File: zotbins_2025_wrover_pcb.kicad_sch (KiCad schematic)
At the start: 6 parts, among them J1 ov2640, J2 hcsr04, J3 hx711, J4 infrared, U1 ESP32-WROVER-E/IE-DEVKIT-C, U2 MCP23017_SP

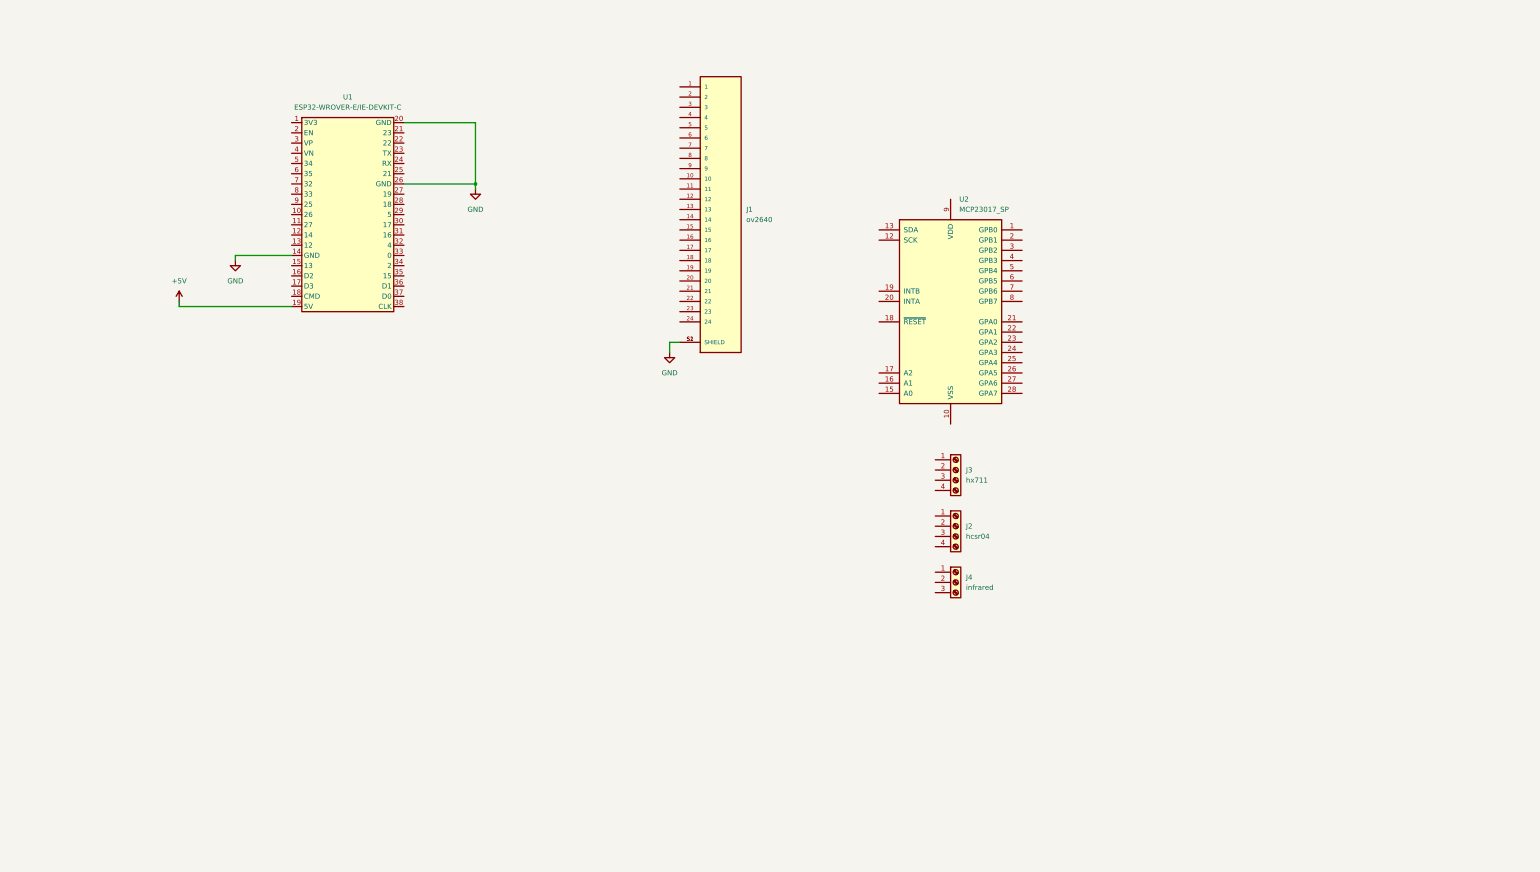
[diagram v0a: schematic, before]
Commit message: Camera and GPIO Expander sch updated
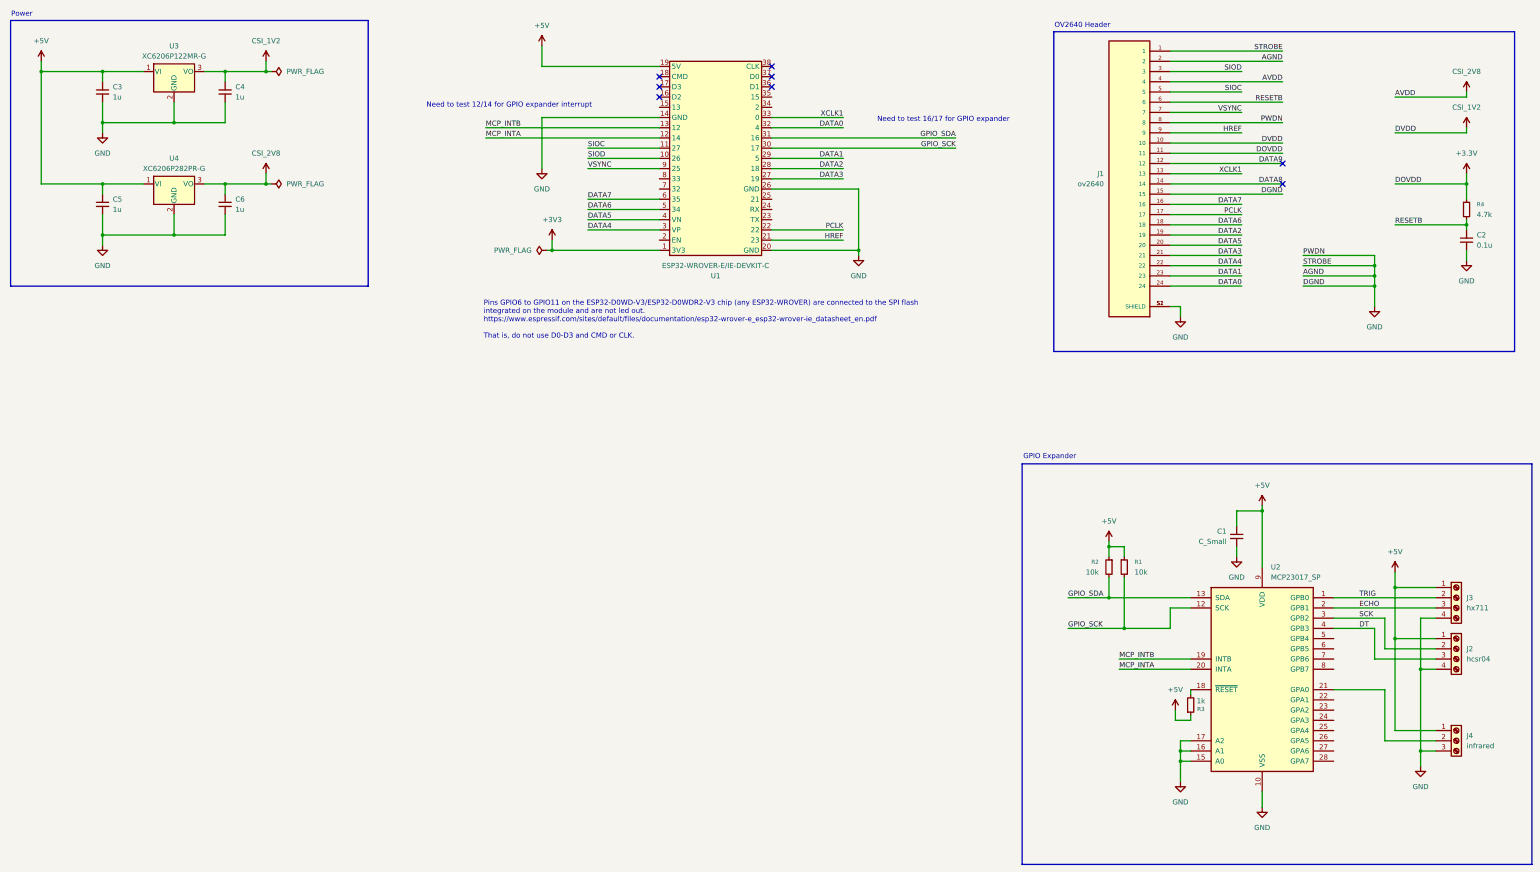
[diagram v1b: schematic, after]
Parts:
- added C1: C_Small, symbol Device:C_Small
- added C2: 0.1u, symbol Device:C_Small
- added C3, C4, C5, C6: 1u, symbol Device:C_Small
- added R1, R2: 10k, symbol Device:R_Small
- added R3: 1k, symbol Device:R_Small
- added R4: 4.7k, symbol Device:R_Small
- added U3: XC6206P122MR-G, Package_TO_SOT_THT:TO-220-3_Vertical, symbol Regulator_Linear:XC6206P122MR-G
- added U4: XC6206P282PR-G, Package_TO_SOT_THT:TO-220-3_Vertical, symbol Regulator_Linear:XC6206P282PR-G
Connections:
- net +5V: now also J2.1 (Pin_1), J3.1 (Pin_1), J4.1 (Pin_1), U2.9 (VDD), C1.1, C3.1, C5.1, R1.1, R2.1, R3.1, U3.1 (VI), U4.1 (VI)
- net GND: now also J1.1, J1.15, J1.2, J1.8, J2.4 (Pin_4), J3.4 (Pin_4), J4.3 (Pin_3), U2.10 (VSS), U2.15 (A0), U2.16 (A1), U2.17 (A2), C1.2, C2.2, C3.2, C4.2, C5.2, C6.2, U3.2 (GND), U4.2 (GND)
- net SCK: now reaches J2.2 (Pin_2)
- net SCK: now also U2.3 (GPB2)
- net DT: now reaches J2.3 (Pin_3)
- net DT: now also U2.4 (GPB3)
- net at J4.2 (Pin_2): now also U2.21 (GPA0)
- net +3V3: now reaches U1.1 (3V3)
- net SIOD: now reaches U1.10 (26)
- net SIOD: now also J1.3
- net SIOC: now reaches U1.11 (27)
- net SIOC: now also J1.5
- net MCP_INTA: now reaches U1.12 (14)
- net MCP_INTA: now also U2.20 (INTA)
- net MCP_INTB: now reaches U1.13 (12)
- net MCP_INTB: now also U2.19 (INTB)
- net HREF: now reaches U1.21 (23)
- net HREF: now also J1.9
- net PCLK: now reaches U1.22
- net PCLK: now also J1.17
- net DATA3: now reaches U1.27 (19)
- net DATA3: now also J1.21
- net DATA2: now reaches U1.28 (18)
- net DATA2: now also J1.19
- net DATA1: now reaches U1.29 (5)
- net DATA1: now also J1.23
- net DATA4: now reaches U1.3 (VP)
- net DATA4: now also J1.22
- net GPIO_SCK: now reaches U1.30 (17)
- net GPIO_SCK: now also U2.12 (SCK), R1.2
- net GPIO_SDA: now reaches U1.31 (16)
- net GPIO_SDA: now also U2.13 (SDA), R2.2
- net DATA0: now reaches U1.32 (4)
- net DATA0: now also J1.24
- net XCLK1: now reaches U1.33 (0)
- net XCLK1: now also J1.13
- net DATA5: now reaches U1.4 (VN)
- net DATA5: now also J1.20
- net DATA6: now reaches U1.5 (34)
- net DATA6: now also J1.18
- net DATA7: now reaches U1.6 (35)
- net DATA7: now also J1.16
- net VSYNC: now reaches U1.9 (25)
- net VSYNC: now also J1.7
- net TRIG: now reaches J3.2 (Pin_2)
- net TRIG: now also U2.1 (GPB0)
- net ECHO: now reaches J3.3 (Pin_3)
- net ECHO: now also U2.2 (GPB1)
- net CSI_1V2: now reaches J1.10
- net CSI_1V2: now also C4.1, U3.3 (VO)
- net +3.3V: now reaches J1.11
- net +3.3V: now also R4.1
- net DATA9: now reaches J1.12
- net DATA8: now reaches J1.14
- net CSI_2V8: now reaches J1.4
- net CSI_2V8: now also C6.1, U4.3 (VO)
- net RESETB: now reaches J1.6
- net RESETB: now also C2.1, R4.2
- net at U2.18 (~{RESET}): now also R3.2
- no-connect marks 0 -> 8
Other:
- note added: "GPIO Expander"
- note added: "Need to test 12/14 for GPIO expander interrupt"
- note added: "Need to test 16/17 for GPIO expander"
- note added: "OV2640 Header"
- note added: "Pins GPIO6 to GPIO11 on the ESP32-D0WD-V3/ESP32-D0WDR2-V3 chip (any ESP32-WROVER) are connected to the SPI flash integrated on the module and are not led out. https://www.espressif.com/sites/default/files/documentation/esp32-wrover-e_esp32-wrover-ie_datasheet_en.pdf That is, do not use D0-D3 and CMD or CLK."
- note added: "Power"
- moved on the sheet: J1, J2, J3, J4, U1, U2

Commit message: All necessary hardware tests completed
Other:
- note removed: "Need to test 12/14 for GPIO expander interrupt"
- note removed: "Need to test 16/17 for GPIO expander"
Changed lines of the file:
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@@
-		)
-	)
-	(text "Need to test 12/14 for GPIO expander interrupt\n"
-		(exclude_from_sim no)
-		(at 143.002 41.402 0)
-		(effects
-			(font
-				(size 1.27 1.27)
-			)
 		)
 	)
@@
 		)
 	)
-	(text "Need to test 16/17 for GPIO expander\n"
-		(exclude_from_sim no)
-		(at 250.952 44.958 0)
-		(effects
-			(font
-				(size 1.27 1.27)
-			)
-		)
-	)
